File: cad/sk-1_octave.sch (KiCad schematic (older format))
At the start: 20 parts, among them U1 4069, U2 74HC74, U3 74LS157

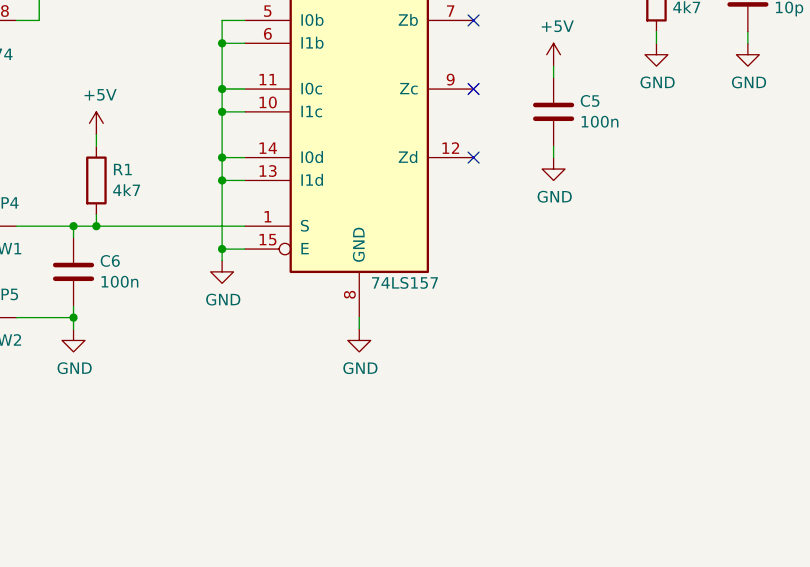
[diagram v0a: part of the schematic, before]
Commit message: 74LSS157 -> 74HCS157. Removed backup files from versioning.
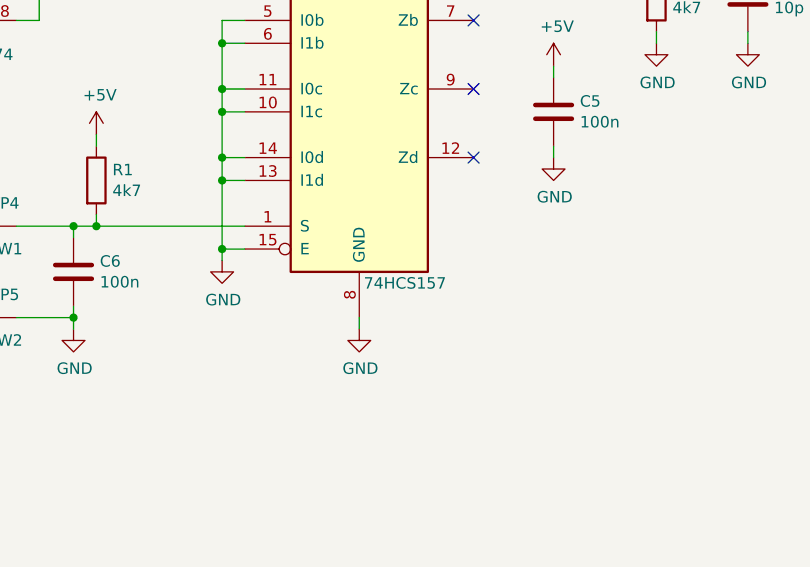
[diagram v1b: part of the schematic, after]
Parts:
- U3: value 74LS157 -> 74HCS157
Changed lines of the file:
@@
 P 6800 3600
 F 0 "U3" H 6950 4350 50  0000 C CNN
-F 1 "74LS157" H 7000 2750 50  0000 C CNN
+F 1 "74HCS157" H 7000 2750 50  0000 C CNN
 F 2 "Package_SO:SOIC-16_3.9x9.9mm_P1.27mm" H 6800 3600 50  0001 C CNN
 F 3 "" H 6800 3600 50  0001 C CNN

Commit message: 74HCS157 -> 74HC157
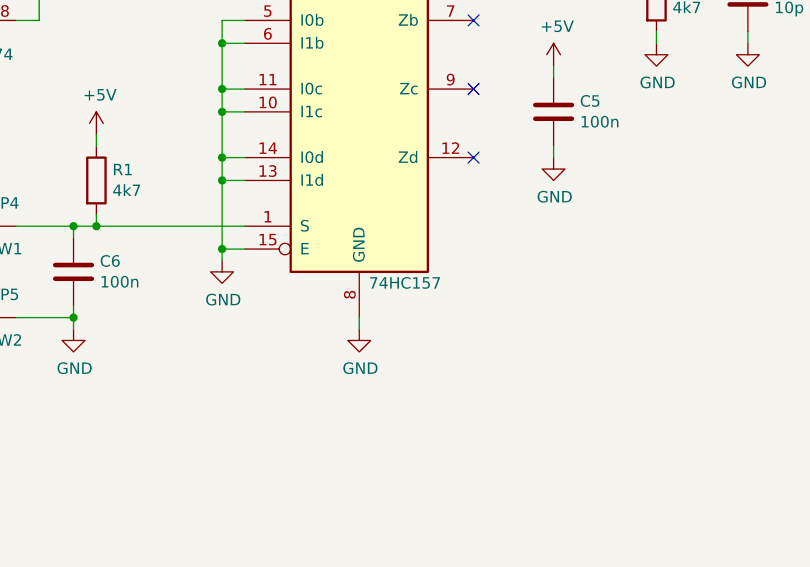
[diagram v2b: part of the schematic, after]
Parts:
- U3: value 74HCS157 -> 74HC157
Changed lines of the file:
@@
 P 6800 3600
 F 0 "U3" H 6950 4350 50  0000 C CNN
-F 1 "74HCS157" H 7000 2750 50  0000 C CNN
+F 1 "74HC157" H 7000 2750 50  0000 C CNN
 F 2 "Package_SO:SOIC-16_3.9x9.9mm_P1.27mm" H 6800 3600 50  0001 C CNN
 F 3 "" H 6800 3600 50  0001 C CNN
